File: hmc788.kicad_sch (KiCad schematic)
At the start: 6 parts, among them U8 HMC788A

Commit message: Darrel Suggestions
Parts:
- removed L1: 6.35u, symbol Device:L_Small
- added FB1: 470 OHM @ 100MHz, Inductor_SMD:L_0402_1005Metric, symbol Device:FerriteBead_Small
- C5, C6: value 10n -> 1n; footprint (none) -> Capacitor_SMD:C_0201_0603Metric; DIGIKEY_PN 1284-1540-1-ND -> (none)
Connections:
- net 5VIN: now also FB1.1
- net RF_{IN}: now also C5.2; no longer C5.1
- net at U8. (RF_{OUT}): now also C5.1; no longer C5.2
- net at C6.2, U8. (RF_{OUT}): now also FB1.2
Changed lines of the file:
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@@
+	)
+	(symbol
+		(lib_id "Device:FerriteBead_Small")
+		(at 152.4 80.01 0)
+		(unit 1)
+		(body_style 1)
+		(exclude_from_sim no)
+		(in_bom yes)
+		(on_board yes)
+		(in_pos_files yes)
+		(dnp no)
+		(property "Reference" "FB1"
+			(at 149.86 78.7018 0)
+			(show_name no)
+			(do_not_autoplace no)
+			(effects
+				(font
+					(size 1.27 1.27)
+				)
+				(justify right)
+			)
+		)
+		(property "Value" "470 OHM @ 100MHz"
+			(at 149.86 81.2418 0)
+			(show_name no)
+			(do_not_autoplace no)
+			(effects
+				(font
+					(size 1.27 1.27)
+				)
+				(justify right)
+			)
+		)
+		(property "Footprint" "Inductor_SMD:L_0402_1005Metric"
+			(at 150.622 80.01 90)
+			(hide yes)
+			(show_name no)
+			(do_not_autoplace no)
+			(effects
+				(font
+					(size 1.27 1.27)
+				)
+			)
+		)
+		(property "Datasheet" ""
+			(at 152.4 80.01 0)
+			(hide yes)
+			(show_name no)
+			(do_not_autoplace no)
+			(effects
+				(font
+					(size 1.27 1.27)
+				)
+			)
+		)
+		(property "Description" "Ferrite bead, small symbol"
+			(at 152.4 80.01 0)
+			(hide yes)
+			(show_name no)
+			(do_not_autoplace no)
+			(effects
+				(font
+					(size 1.27 1.27)
+				)
+			)
+		)
+		(property "DIGIKEY_PN" "490-5198-1-ND"
+			(at 152.4 80.01 0)
+			(hide yes)
+			(show_name no)
+			(do_not_autoplace no)
+			(effects
+				(font
+					(size 1.27 1.27)
+				)
+			)
+		)
+		(pin "1"
+		)
+		(pin "2"
+		)
+		(instances
+			(project "huskypointofload"
+				(path "/eb9c972b-d134-41da-be97-ece3f463f7e0/cb2bed6b-53a5-4f58-b70f-ffa107cbb07d/3680bb14-ef6d-491f-878c-9613c4989b3b"
+					(reference "FB1")
+					(unit 1)
+				)
+				(path "/eb9c972b-d134-41da-be97-ece3f463f7e0/d592dca6-985b-424e-980b-4b036b0ee281/ac278918-a47b-404c-8a96-6090a2d8d859"
+					(reference "FB2")
+					(unit 1)
+				)
+				(path "/eb9c972b-d134-41da-be97-ece3f463f7e0/ff4f07c4-e191-4e61-a9ef-d50cbe59545f/ac278918-a47b-404c-8a96-6090a2d8d859"
+					(reference "FB5")
+					(unit 1)
+				)
+			)
+		)
 	)
 	(symbol
@@
 		(dnp no)
 		(fields_autoplaced yes)
-		(property "Reference" "#PWR027"
+		(property "Reference" "#PWR029"
 			(at 171.45 93.98 0)
 			(hide yes)
@@
 			(project "huskypointofload"
 				(path "/eb9c972b-d134-41da-be97-ece3f463f7e0/cb2bed6b-53a5-4f58-b70f-ffa107cbb07d/3680bb14-ef6d-491f-878c-9613c4989b3b"
-					(reference "#PWR027")
+					(reference "#PWR029")
 					(unit 1)
 				)
 				(path "/eb9c972b-d134-41da-be97-ece3f463f7e0/d592dca6-985b-424e-980b-4b036b0ee281/ac278918-a47b-404c-8a96-6090a2d8d859"
-					(reference "#PWR091")
+					(reference "#PWR093")
 					(unit 1)
 				)
 				(path "/eb9c972b-d134-41da-be97-ece3f463f7e0/ff4f07c4-e191-4e61-a9ef-d50cbe59545f/ac278918-a47b-404c-8a96-6090a2d8d859"
-					(reference "#PWR0312")
+					(reference "#PWR0313")
 					(unit 1)
 				)
@@
 				)
 				(path "/eb9c972b-d134-41da-be97-ece3f463f7e0/ff4f07c4-e191-4e61-a9ef-d50cbe59545f/ac278918-a47b-404c-8a96-6090a2d8d859"
-					(reference "U43")
-					(unit 1)
-				)
-			)
-		)
-	)
-	(symbol
-		(lib_id "Device:C_Small")
-		(at 120.65 101.6 90)
-		(mirror x)
-		(unit 1)
-		(body_style 1)
-		(exclude_from_sim no)
-		(in_bom yes)
-		(on_board yes)
-		(in_pos_files yes)
-		(dnp no)
-		(property "Reference" "C5"
-			(at 120.65 106.934 90)
-			(show_name no)
-			(do_not_autoplace no)
-			(effects
-				(font
-					(size 1.27 1.27)
-				)
-			)
-		)
-		(property "Value" "10n"
-			(at 120.65 104.394 90)
-			(show_name no)
-			(do_not_autoplace no)
-			(effects
-				(font
-					(size 1.27 1.27)
-				)
-			)
-		)
-		(property "Footprint" ""
-			(at 120.65 101.6 0)
-			(hide yes)
-			(show_name no)
-			(do_not_autoplace no)
-			(effects
-				(font
-					(size 1.27 1.27)
-				)
-			)
-		)
-		(property "Datasheet" ""
-			(at 120.65 101.6 0)
-			(hide yes)
-			(show_name no)
-			(do_not_autoplace no)
-			(effects
-				(font
-					(size 1.27 1.27)
-				)
-			)
-		)
-		(property "Description" "Unpolarized capacitor, small symbol"
-			(at 120.65 101.6 0)
-			(hide yes)
-			(show_name no)
-			(do_not_autoplace no)
-			(effects
-				(font
-					(size 1.27 1.27)
-				)
-			)
-		)
-		(property "DIGIKEY_PN" "1284-1540-1-ND"
-			(at 120.65 101.6 90)
-			(hide yes)
-			(show_name no)
-			(do_not_autoplace no)
-			(effects
-				(font
-					(size 1.27 1.27)
-				)
-			)
-		)
-		(pin "2"
-		)
-		(pin "1"
-		)
-		(instances
-			(project "huskypointofload"
-				(path "/eb9c972b-d134-41da-be97-ece3f463f7e0/cb2bed6b-53a5-4f58-b70f-ffa107cbb07d/3680bb14-ef6d-491f-878c-9613c4989b3b"
-					(reference "C5")
-					(unit 1)
-				)
-				(path "/eb9c972b-d134-41da-be97-ece3f463f7e0/d592dca6-985b-424e-980b-4b036b0ee281/ac278918-a47b-404c-8a96-6090a2d8d859"
-					(reference "C65")
-					(unit 1)
-				)
-				(path "/eb9c972b-d134-41da-be97-ece3f463f7e0/ff4f07c4-e191-4e61-a9ef-d50cbe59545f/ac278918-a47b-404c-8a96-6090a2d8d859"
-					(reference "C270")
+					(reference "U44")
 					(unit 1)
 				)
@@
 				)
 				(path "/eb9c972b-d134-41da-be97-ece3f463f7e0/ff4f07c4-e191-4e61-a9ef-d50cbe59545f/ac278918-a47b-404c-8a96-6090a2d8d859"
-					(reference "C272")
+					(reference "C276")
 					(unit 1)
 				)
@@
 	)
 	(symbol
-		(lib_id "Device:L_Small")
-		(at 152.4 80.01 0)
-		(mirror y)
+		(lib_id "Device:C_Small")
+		(at 120.65 101.6 270)
 		(unit 1)
 		(body_style 1)
@@
 		(in_pos_files yes)
 		(dnp no)
-		(property "Reference" "L1"
-			(at 151.13 78.7399 0)
-			(show_name no)
-			(do_not_autoplace no)
-			(effects
-				(font
-					(size 1.27 1.27)
-				)
-				(justify left)
-			)
-		)
-		(property "Value" "6.35u"
-			(at 151.13 81.2799 0)
-			(show_name no)
-			(do_not_autoplace no)
-			(effects
-				(font
-					(size 1.27 1.27)
-				)
-				(justify left)
-			)
-		)
-		(property "Footprint" ""
-			(at 152.4 80.01 0)
+		(property "Reference" "C5"
+			(at 120.65 106.934 90)
+			(show_name no)
+			(do_not_autoplace no)
+			(effects
+				(font
+					(size 1.27 1.27)
+				)
+			)
+		)
+		(property "Value" "1n"
+			(at 120.65 104.394 90)
+			(show_name no)
+			(do_not_autoplace no)
+			(effects
+				(font
+					(size 1.27 1.27)
+				)
+			)
+		)
+		(property "Footprint" "Capacitor_SMD:C_0201_0603Metric"
+			(at 120.65 101.6 0)
 			(hide yes)
 			(show_name no)
@@
 		)
 		(property "Datasheet" ""
-			(at 152.4 80.01 0)
-			(hide yes)
-			(show_name no)
-			(do_not_autoplace no)
-			(effects
-				(font
-					(size 1.27 1.27)
-				)
-			)
-		)
-		(property "Description" "Inductor, small symbol"
-			(at 152.4 80.01 0)
-			(hide yes)
-			(show_name no)
-			(do_not_autoplace no)
-			(effects
-				(font
-					(size 1.27 1.27)
-				)
-			)
+			(at 120.65 101.6 0)
+			(hide yes)
+			(show_name no)
+			(do_not_autoplace no)
+			(effects
+				(font
+					(size 1.27 1.27)
+				)
+			)
+		)
+		(property "Description" "Unpolarized capacitor, small symbol"
+			(at 120.65 101.6 0)
+			(hide yes)
+			(show_name no)
+			(do_not_autoplace no)
+			(effects
+				(font
+					(size 1.27 1.27)
+				)
+			)
+		)
+		(property "DIGIKEY_PN" ""
+			(at 120.65 101.6 90)
+			(hide yes)
+			(show_name no)
+			(do_not_autoplace no)
+			(effects
+				(font
+					(size 1.27 1.27)
+				)
+			)
+		)
+		(pin "2"
 		)
 		(pin "1"
-		)
-		(pin "2"
 		)
 		(instances
 			(project "huskypointofload"
 				(path "/eb9c972b-d134-41da-be97-ece3f463f7e0/cb2bed6b-53a5-4f58-b70f-ffa107cbb07d/3680bb14-ef6d-491f-878c-9613c4989b3b"
-					(reference "L1")
+					(reference "C5")
 					(unit 1)
 				)
 				(path "/eb9c972b-d134-41da-be97-ece3f463f7e0/d592dca6-985b-424e-980b-4b036b0ee281/ac278918-a47b-404c-8a96-6090a2d8d859"
-					(reference "L4")
+					(reference "C65")
 					(unit 1)
 				)
 				(path "/eb9c972b-d134-41da-be97-ece3f463f7e0/ff4f07c4-e191-4e61-a9ef-d50cbe59545f/ac278918-a47b-404c-8a96-6090a2d8d859"
-					(reference "L12")
+					(reference "C274")
 					(unit 1)
 				)
@@
 				)
 				(path "/eb9c972b-d134-41da-be97-ece3f463f7e0/ff4f07c4-e191-4e61-a9ef-d50cbe59545f/ac278918-a47b-404c-8a96-6090a2d8d859"
-					(reference "C273")
+					(reference "C277")
 					(unit 1)
 				)
@@
 		(dnp no)
 		(fields_autoplaced yes)
-		(property "Reference" "#PWR026"
+		(property "Reference" "#PWR028"
 			(at 139.7 125.73 0)
 			(hide yes)
@@
 			(project "huskypointofload"
 				(path "/eb9c972b-d134-41da-be97-ece3f463f7e0/cb2bed6b-53a5-4f58-b70f-ffa107cbb07d/3680bb14-ef6d-491f-878c-9613c4989b3b"
-					(reference "#PWR026")
+					(reference "#PWR028")
 					(unit 1)
 				)
 				(path "/eb9c972b-d134-41da-be97-ece3f463f7e0/d592dca6-985b-424e-980b-4b036b0ee281/ac278918-a47b-404c-8a96-6090a2d8d859"
-					(reference "#PWR090")
+					(reference "#PWR092")
 					(unit 1)
 				)
 				(path "/eb9c972b-d134-41da-be97-ece3f463f7e0/ff4f07c4-e191-4e61-a9ef-d50cbe59545f/ac278918-a47b-404c-8a96-6090a2d8d859"
-					(reference "#PWR0311")
+					(reference "#PWR0312")
 					(unit 1)
 				)
@@
 			)
 		)
-		(property "Value" "10n"
+		(property "Value" "1n"
 			(at 158.75 104.394 90)
 			(show_name no)
@@
 			)
 		)
-		(property "Footprint" ""
+		(property "Footprint" "Capacitor_SMD:C_0201_0603Metric"
 			(at 158.75 101.6 0)
 			(hide yes)
@@
 			)
 		)
-		(property "DIGIKEY_PN" "1284-1540-1-ND"
+		(property "DIGIKEY_PN" ""
 			(at 158.75 101.6 90)
 			(hide yes)
@@
 				)
 				(path "/eb9c972b-d134-41da-be97-ece3f463f7e0/ff4f07c4-e191-4e61-a9ef-d50cbe59545f/ac278918-a47b-404c-8a96-6090a2d8d859"
-					(reference "C271")
-					(unit 1)
-				)
+					(reference "C275")
+					(unit 1)
+				)

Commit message: Passive footprint pass
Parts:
- C7, C8: footprint (none) -> Capacitor_SMD:C_0402_1005Metric
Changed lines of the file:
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@@
 			)
 		)
-		(property "Footprint" ""
+		(property "Footprint" "Capacitor_SMD:C_0402_1005Metric"
 			(at 161.29 80.01 0)
 			(hide yes)
@@
 			)
 		)
-		(property "Footprint" ""
+		(property "Footprint" "Capacitor_SMD:C_0402_1005Metric"
 			(at 171.45 80.01 0)
 			(hide yes)

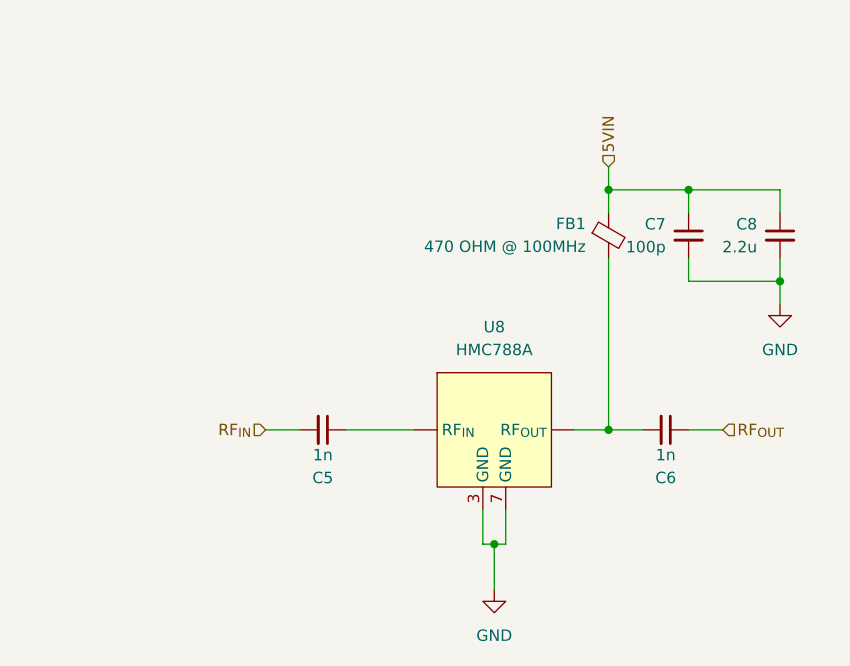
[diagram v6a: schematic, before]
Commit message: add NC and fix ERC
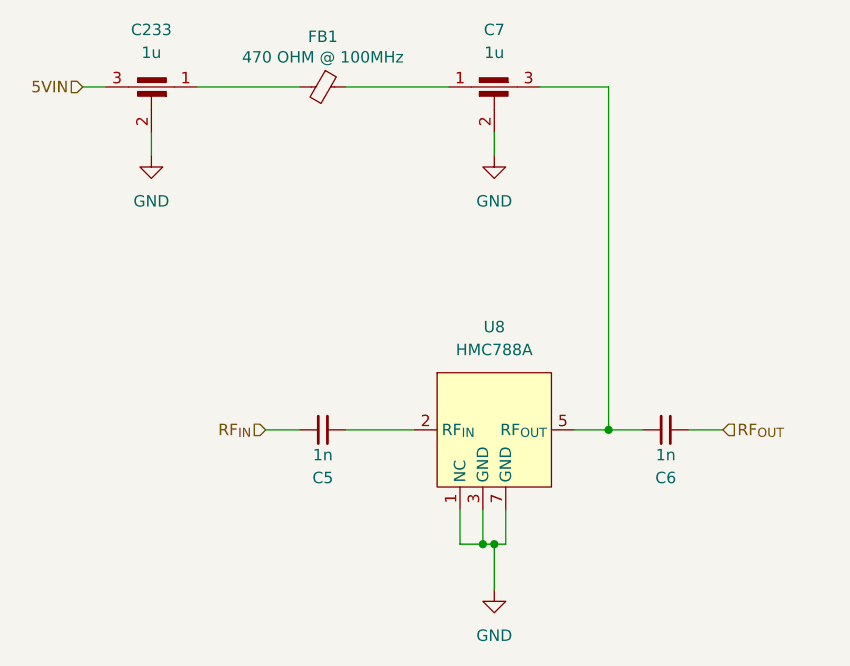
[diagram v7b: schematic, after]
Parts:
- removed C7: 100p, Capacitor_SMD:C_0402_1005Metric, symbol Device:C_Small
- removed C8: 2.2u, Capacitor_SMD:C_0402_1005Metric, symbol Device:C_Small
- added C233, C7: 1u, symbol Device:C_Feedthrough
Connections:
- net 5VIN: now also C233.3; no longer FB1.1
- net GND: now also U8.1 (NC), U8.4 (NC), U8.6 (NC), C233.2, C7.2
- net at C5.1: now also U8.2 (RF_{IN}); no longer U8. (RF_{OUT})
- new net: C7.1, FB1.1
- new net: C233.1, FB1.2
- new net: C6.2, C7.3, U8.5 (RF_{OUT})
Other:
- moved on the sheet: FB1
